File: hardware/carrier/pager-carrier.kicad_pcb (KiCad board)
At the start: 2 copper layers, 85 x 52 mm, 107 parts, among them J1 USB4235, J2 BATTERY, J3 PANEL, J4 CARDKB, J5 FRONTLIGHT, J6 MSG_LED, J7 HAPTIC, M1 Walter, Q1 DMG2305UX-7, Q2 UMH3N, Q4 2N7002, SW1 JS102011SAQN, U1 BQ25185DLHR, U10 MAX17048G+T10, U3 TPS62840DLCR, U4 TPS22917DBV, U5 CP2102N-A02-GQFN24, U6 SN74LVC2G126DCUR, U7 LIS2DW12TR, U8 NSI45020AT1G, U9 DRV2605LDGSR

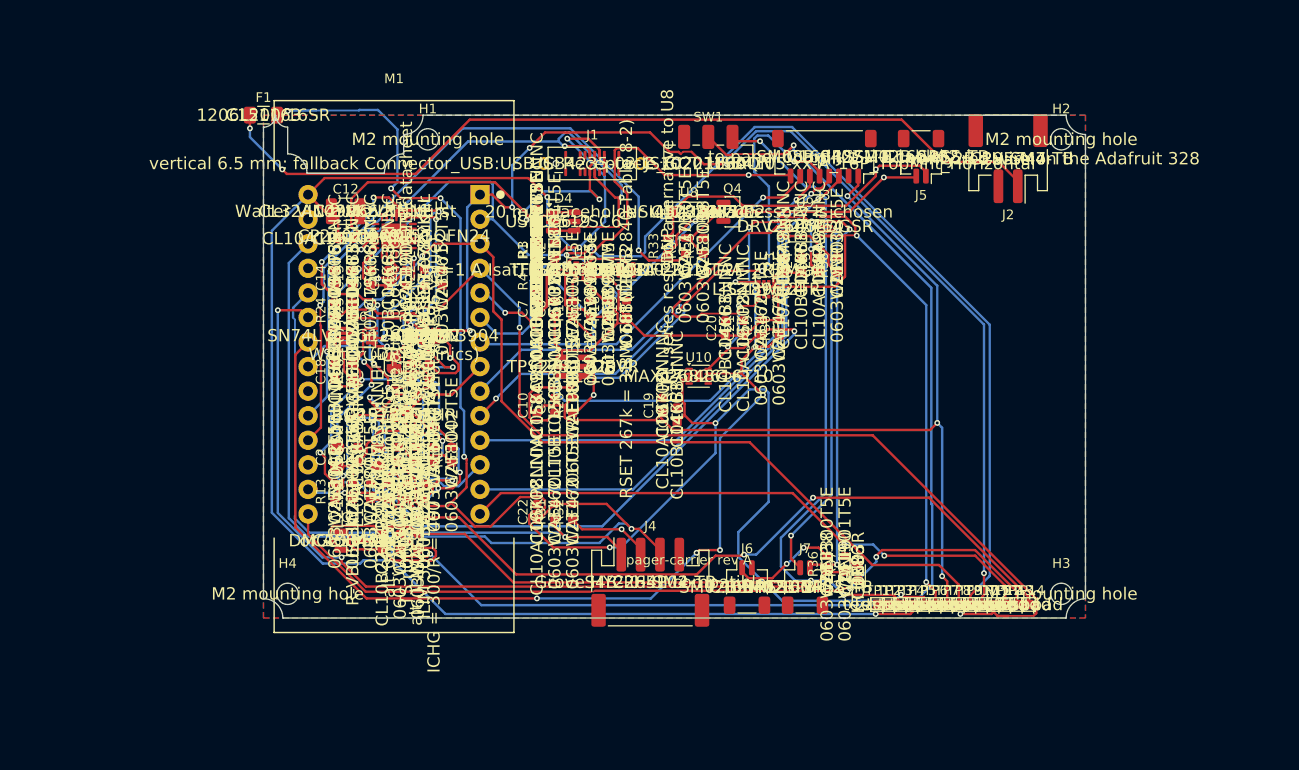
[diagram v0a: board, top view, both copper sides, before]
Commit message: hardware/carrier: route both boards (Freerouting via pcbnew DSN/SES), DRC-fix pass -- NC-pin nets, 1.7 mm Walter pads, edge keep-outs, courtyard and BOM-attribute sync; panel fully routed (silk warnings only), carrier one USB_DM link unrouted plus a few courtyard nits listed in the README; board PDFs exported
Co-Authored-By: Claude Fable 5.1 <noreply@anthropic.com>
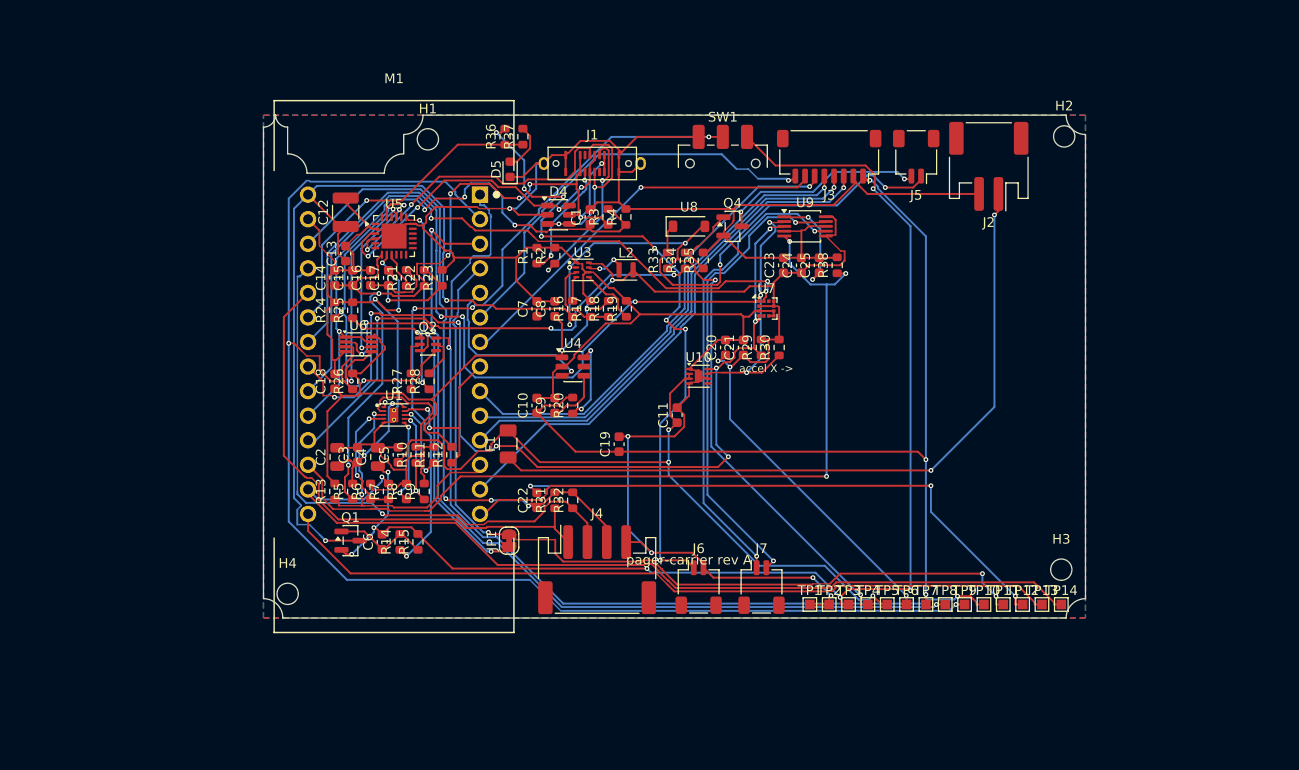
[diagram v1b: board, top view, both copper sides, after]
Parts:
- C1, C10, C11, C13, C14, C15, C16, C17, C18, C19, C20, C21, C22, C23, C24, C25, C3, C5, C6, C7, C8, C9: footprint C_0603_1608Metric -> Capacitor_SMD:C_0603_1608Metric
- C12: footprint C_1210_3225Metric -> Capacitor_SMD:C_1210_3225Metric
- C2, C4: footprint C_0805_2012Metric -> Capacitor_SMD:C_0805_2012Metric
- D4, U4: footprint SOT-23-6 -> Package_TO_SOT_SMD:SOT-23-6
- D5: footprint LED_0603_1608Metric -> LED_SMD:LED_0603_1608Metric
- F1: footprint Fuse_1206_3216Metric -> Fuse:Fuse_1206_3216Metric
- H1, H2, H3, H4: footprint MountingHole_2.2mm_M2 -> MountingHole:MountingHole_2.2mm_M2
- J1: footprint USB_C_Receptacle_GCT_USB4235_Vertical -> pager-carrier:USB_C_Receptacle_GCT_USB4235_Vertical
- J2: footprint JST_PH_S2B-PH-SM4-TB_1x02-1MP_P2.00mm_Horizontal -> Connector_JST:JST_PH_S2B-PH-SM4-TB_1x02-1MP_P2.00mm_Horizontal
- J3: footprint JST_SH_SM08B-SRSS-TB_1x08-1MP_P1.00mm_Horizontal -> Connector_JST:JST_SH_SM08B-SRSS-TB_1x08-1MP_P1.00mm_Horizontal
- J4: footprint JST_PH_S4B-PH-SM4-TB_1x04-1MP_P2.00mm_Horizontal -> Connector_JST:JST_PH_S4B-PH-SM4-TB_1x04-1MP_P2.00mm_Horizontal
- J5, J6, J7: footprint JST_SH_SM02B-SRSS-TB_1x02-1MP_P1.00mm_Horizontal -> Connector_JST:JST_SH_SM02B-SRSS-TB_1x02-1MP_P1.00mm_Horizontal
- JP1: footprint SolderJumper-2_P1.3mm_Bridged_RoundedPad1.0x1.5mm -> Jumper:SolderJumper-2_P1.3mm_Bridged_RoundedPad1.0x1.5mm
- L2: footprint L_Murata_DFE201610P -> Inductor_SMD:L_Murata_DFE201610P
- M1: footprint Walter_Module_2x14_THT -> pager-carrier:Walter_Module_2x14_THT
- Q1, Q4: footprint SOT-23 -> Package_TO_SOT_SMD:SOT-23
- Q2: footprint SOT-363_SC-70-6 -> Package_TO_SOT_SMD:SOT-363_SC-70-6
- R1, R10, R11, R12, R13, R14, R15, R16, R17, R18, R19, R2, R20, R21, R22, R23, R24, R25, R26, R27, R28, R29, R3, R30, R31, R32, R33, R34, R35, R36, R37, R38, R4, R5, R6, R7, R8, R9: footprint R_0603_1608Metric -> Resistor_SMD:R_0603_1608Metric
- SW1: footprint SW_SPDT_CK_JS102011SAQN -> Button_Switch_SMD:SW_SPDT_CK_JS102011SAQN
- TP1, TP10, TP11, TP12, TP13, TP14, TP2, TP3, TP4, TP5, TP6, TP7, TP8, TP9: footprint TestPoint_Pad_1.0x1.0mm -> TestPoint:TestPoint_Pad_1.0x1.0mm
- U1: footprint BQ25185_WSON-10_DLH0010A_2.2x2mm_P0.4mm_EP0.9x1.5mm -> pager-carrier:BQ25185_WSON-10_DLH0010A_2.2x2mm_P0.4mm_EP0.9x1.5mm
- U10: footprint TDFN-8-1EP_2x2mm_P0.5mm_EP0.8x1.2mm -> Package_DFN_QFN:TDFN-8-1EP_2x2mm_P0.5mm_EP0.8x1.2mm
- U3: footprint TPS62840_VSON-HR-8_DLC0008B_1.5x2mm_P0.5mm -> pager-carrier:TPS62840_VSON-HR-8_DLC0008B_1.5x2mm_P0.5mm
- U5: footprint QFN-24-1EP_4x4mm_P0.5mm_EP2.6x2.6mm -> Package_DFN_QFN:QFN-24-1EP_4x4mm_P0.5mm_EP2.6x2.6mm
- U6: footprint VSSOP-8_2.3x2mm_P0.5mm -> Package_SO:VSSOP-8_2.3x2mm_P0.5mm
- U7: footprint LGA-12_2x2mm_P0.5mm -> Package_LGA:LGA-12_2x2mm_P0.5mm
- U8: footprint D_SOD-123 -> Diode_SMD:D_SOD-123
- U9: footprint TSSOP-10_3x3mm_P0.5mm -> Package_SO:TSSOP-10_3x3mm_P0.5mm
- moved R36 55.3 mm to (25.0, 2.23)
- moved R37 55.3 mm to (26.8, 2.23)
- moved D5 55.1 mm to (25.5, 5.60)
- moved F1 42.4 mm to (25.3, 34.0), turned to 90 degrees
- moved JP1 21.9 mm to (25.4, 44.0)
- moved R4 11.4 mm to (37.5, 10.5)
- moved R3 8.08 mm to (35.6, 10.5)
- moved TP1 7.00 mm to (56.5, 50.6)
- moved TP2 6.20 mm to (58.5, 50.6)
- moved C19 6.02 mm to (36.8, 34.0)
- moved J4 5.65 mm to (34.5, 47.0)
- moved C1 5.50 mm to (33.8, 10.5)
- moved TP3 5.40 mm to (60.5, 50.6)
- moved J6 5.00 mm to (45.0, 48.8)
- moved TP4 4.60 mm to (62.5, 50.6)
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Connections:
- J1 pad A8: (no net) -> unconnected-(J1-SBU1-PadA8)
- J1 pad B8: (no net) -> unconnected-(J1-SBU2-PadB8)
- U10 pad 5: (no net) -> unconnected-(U10-~{ALRT}-Pad5)
- U4 pad 5: (no net) -> unconnected-(U4-QOD-Pad5)
- U5 pad 1: (no net) -> unconnected-(U5-~{RI}/CLK-Pad1)
- U5 pad 10: (no net) -> unconnected-(U5-NC-Pad10)
- U5 pad 11: (no net) -> unconnected-(U5-~{WAKEUP}/GPIO.3-Pad11)
- U5 pad 12: (no net) -> unconnected-(U5-RS485/GPIO.2-Pad12)
- U5 pad 13: (no net) -> unconnected-(U5-~{RXT}/GPIO.1-Pad13)
- U5 pad 14: (no net) -> unconnected-(U5-~{TXT}/GPIO.0-Pad14)
- U5 pad 15: (no net) -> unconnected-(U5-~{SUSPEND}-Pad15)
- U5 pad 16: (no net) -> unconnected-(U5-NC-Pad16)
- U5 pad 17: (no net) -> unconnected-(U5-SUSPEND-Pad17)
- U5 pad 22: (no net) -> unconnected-(U5-~{DSR}-Pad22)
- U5 pad 24: (no net) -> unconnected-(U5-~{DCD}-Pad24)
- U7 pad 11: (no net) -> unconnected-(U7-INT2-Pad11)
- U7 pad 5: (no net) -> unconnected-(U7-NC-Pad5)
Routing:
- net GND: track 0.00 -> 367.0 mm, vias 0 -> 9
- net VBAT: track 178.2 -> 87.8 mm, vias 9 -> 3
- net VBUS: track 1.74 -> 86.9 mm, vias 0 -> 8
- net HAPTIC_EN: track 7.67 -> 89.4 mm, vias 1 -> 3
- net ACC_INT1: track 0.00 -> 69.8 mm, vias 0 -> 3
- net LED_A: track 11.2 -> 69.9 mm, vias 2 -> 8
- net MSG_LED: track 87.2 -> 33.2 mm, vias 2 -> 1
- net VBUS_DET: track 11.4 -> 63.1 mm, vias 1 -> 4
- net KBD_SDA: track 8.90 -> 59.4 mm
- net SW_COM: track 119.9 -> 70.1 mm, vias 2 -> 4
- net EPD_DC: track 86.6 -> 49.3 mm
- net SYS_SW: track 198.3 -> 164.3 mm, vias 6 -> 7
- net ACC_SDA: track 121.0 -> 99.6 mm, vias 5 -> 8
- net FL_PWM: track 71.2 -> 52.0 mm, vias 2 -> 3
- net ESP_EN: track 117.2 -> 98.1 mm, vias 5 -> 2
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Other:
- board text removed: "X"

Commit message: hardware/carrier: front light is the GDEY029T94-FL03 (6-pin flex -> FH34SRJ-6S on the panel board, anode/cathode over a 10-way SH cable, 33R 1206 + Q4 PWM drive replaces the NSI45020), front-light button SW2 on IO4 (FL_BTN), low-profile pass (FH34SRJ 1.0 mm ZIFs, 2 x 100uF 0805 instead of the 2.5 mm 1210, part-height table), sleep-current audit (Q1 gate pull-up 100k -> 2.2M: 38 -> 1.9 uA; SN74LVC2G126 moved to the bus-powered BRG_VDD rail: 0 on battery; table in the README), TPS62840 has no fixed-3.3 V variant (README). Custom FH34SRJ footprints from the Hirose catalog; LCSC numbers via the JLCPCB parts API. Both boards re-placed and re-routed: 0 unconnected, 0 clearance/courtyard errors, silk notes only; ERC 0/0; exports refreshed (owner, 17 Oct 2026)
Co-Authored-By: Claude Fable 5.1 <noreply@anthropic.com>
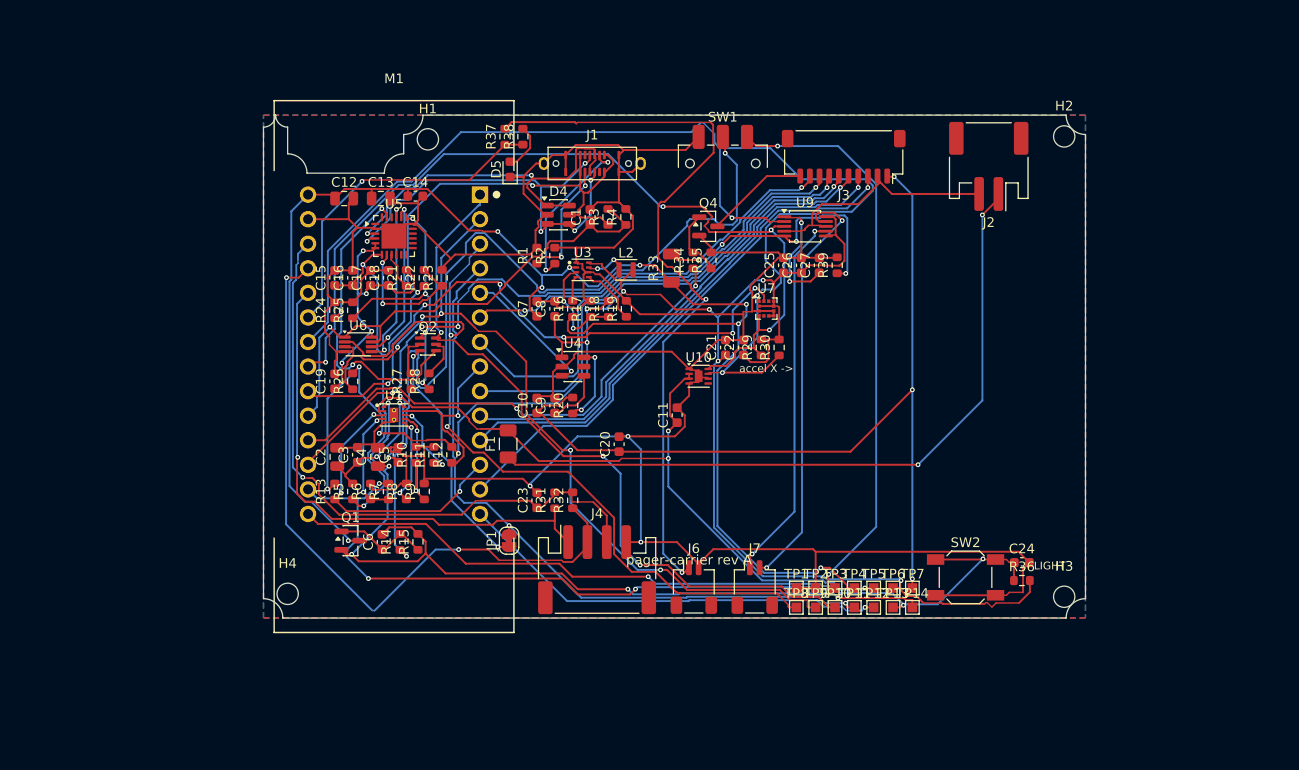
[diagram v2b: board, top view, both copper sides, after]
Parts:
- removed J5: FRONTLIGHT, Connector_JST:JST_SH_SM02B-SRSS-TB_1x02-1MP_P1.00mm_Horizontal
- removed U8: NSI45020AT1G, Diode_SMD:D_SOD-123
- added C26: 100nF, Capacitor_SMD:C_0603_1608Metric, F.Cu at (55.6, 15.5)
- added C27: 1uF, Capacitor_SMD:C_0603_1608Metric, F.Cu at (57.5, 15.5)
- added R39: 100k, Resistor_SMD:R_0603_1608Metric, F.Cu at (59.3, 15.5)
- added SW2: SKQGAFE010, Button_Switch_SMD:SW_SPST_SKQG_WithoutStem, F.Cu at (72.6, 47.8)
- C12: footprint Capacitor_SMD:C_1210_3225Metric -> Capacitor_SMD:C_0805_2012Metric
- C13: value 10uF -> 100uF; footprint Capacitor_SMD:C_0603_1608Metric -> Capacitor_SMD:C_0805_2012Metric
- C14: value 4.7uF -> 10uF
- C15, C17: value 100nF -> 4.7uF
- C16: value 4.7uF -> 100nF
- C19, C21: value 10uF -> 100nF
- C20: value 100nF -> 10uF
- C23: value 1uF -> 10uF
- J3: footprint Connector_JST:JST_SH_SM08B-SRSS-TB_1x08-1MP_P1.00mm_Horizontal -> Connector_JST:JST_SH_SM10B-SRSS-TB_1x10-1MP_P1.00mm_Horizontal
- R15: value 100k -> 2.2M
- R33: value DNP -> 33R; footprint Resistor_SMD:R_0603_1608Metric -> Resistor_SMD:R_1206_3216Metric
- R36: value 330R -> 100k
- R37: value 1k -> 330R
- R38: value 100k -> 1k
- TP13: value TP_IO4 -> FL_BTN
- moved R36 70.5 mm to (78.4, 48.1), turned to 0 degrees
- moved C24 38.3 mm to (78.4, 46.3), turned to 0 degrees
- moved C23 35.2 mm to (28.3, 39.8)
- moved R38 35.1 mm to (26.8, 2.23)
- moved C19 30.1 mm to (7.38, 27.5)
- moved C22 26.6 mm to (49.6, 24.0)
- moved TP13 15.4 mm to (65.1, 50.9)
- moved TP14 15.4 mm to (67.1, 50.9)
- moved TP10 15.4 mm to (59.1, 50.9)
- moved TP11 15.4 mm to (61.1, 50.9)
- moved TP12 15.4 mm to (63.1, 50.9)
- moved TP8 15.4 mm to (55.1, 50.9)
- moved TP9 15.4 mm to (57.1, 50.9)
- moved C20 14.9 mm to (36.8, 34.0)
- moved C18 12.1 mm to (12.9, 16.8)
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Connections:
- C14 pad 1: VBUS -> SYS_SW
- C16 pad 1: BRG_VDD -> VBUS
- C18 pad 1: 3V3 -> BRG_VDD
- C19 pad 1: 3V3_EPD -> BRG_VDD
- C20 pad 1: 3V3 -> 3V3_EPD
- C22 pad 1: 3V3_OUT -> 3V3
- C23 pad 1: 3V3 -> 3V3_OUT
- C24 pad 1: 3V3 -> FL_BTN
- C25 pad 1: HAP_REG -> 3V3
- M1 pad 15: TP_IO4 -> FL_BTN
- R36 pad 1: MSG_LED -> FL_BTN
- R36 pad 2: LED_A -> 3V3
- R37 pad 2: LED_D5 -> LED_A
- R38 pad 1: HAPTIC_EN -> MSG_LED
- R38 pad 2: GND -> LED_D5
- TP13 pad 1: TP_IO4 -> FL_BTN
- U6 pad 8: 3V3 -> BRG_VDD
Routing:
- net FL_BTN: track 0.00 -> 87.1 mm, vias 0 -> 3
- net TP_IO4: track 81.5 -> 0.00 mm
- net ESP_RX0: track 144.1 -> 87.1 mm, vias 2 -> 5
- net 3V3: track 158.0 -> 190.4 mm, vias 6 -> 11
- net ACC_SCL: track 106.0 -> 129.5 mm, vias 6 -> 3
- net ESP_EN: track 98.1 -> 75.7 mm, vias 2 -> 3
- net FL_ANODE: track 40.4 -> 18.6 mm
- net ESP_TX0: track 104.4 -> 83.4 mm, vias 5 -> 2
- net BRG_VDD: track 8.04 -> 28.3 mm, vias 0 -> 4
- net TP_IO1: track 64.8 -> 45.1 mm, vias 2 -> 1
- net SW_COM: track 70.1 -> 89.4 mm, vias 4 -> 2
- net KBD_PWR_N: track 89.5 -> 72.1 mm, vias 3 -> 2
- net TP_IO5: track 94.1 -> 77.6 mm, vias 1 -> 4
- net GND: track 367.0 -> 382.6 mm, vias 9 -> 3
- net KBD_SDA: track 59.4 -> 71.4 mm, vias 1 -> 2
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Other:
- board text added: "LIGHT"
